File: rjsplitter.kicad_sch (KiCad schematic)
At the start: 8 parts, among them J1 8P8C, J2 8P8C, J3 8P8C, J4 8P8C, J5 8P8C

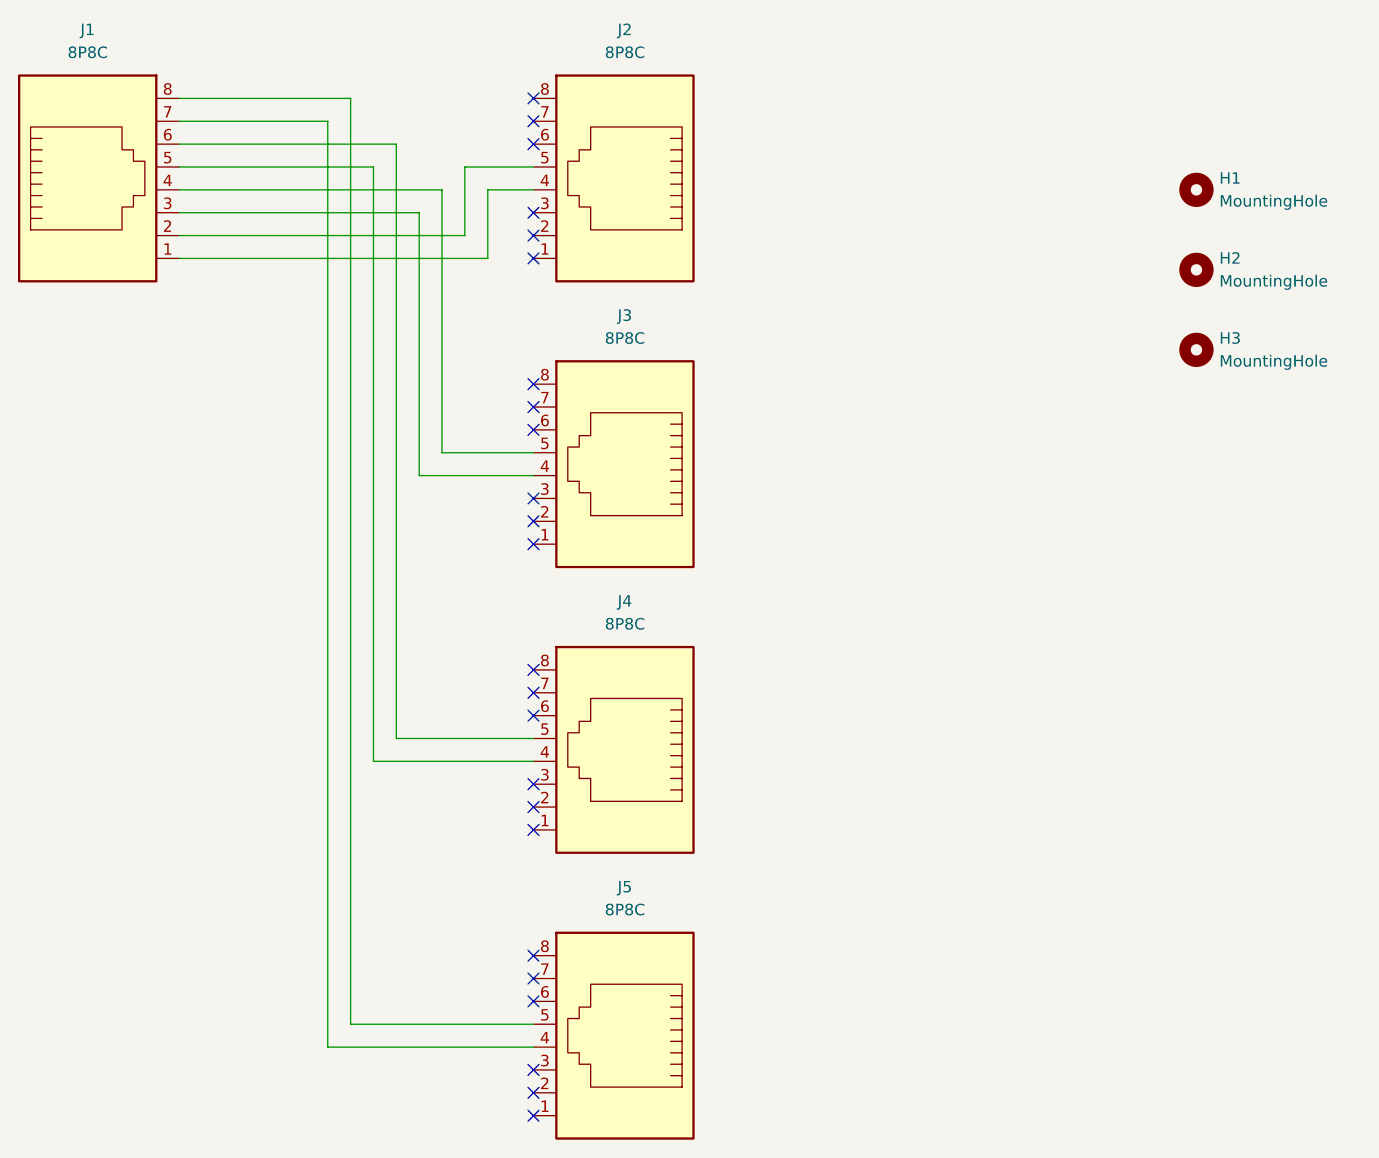
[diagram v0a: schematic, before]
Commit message: Switch to a mix of RJ45 and RJ11.
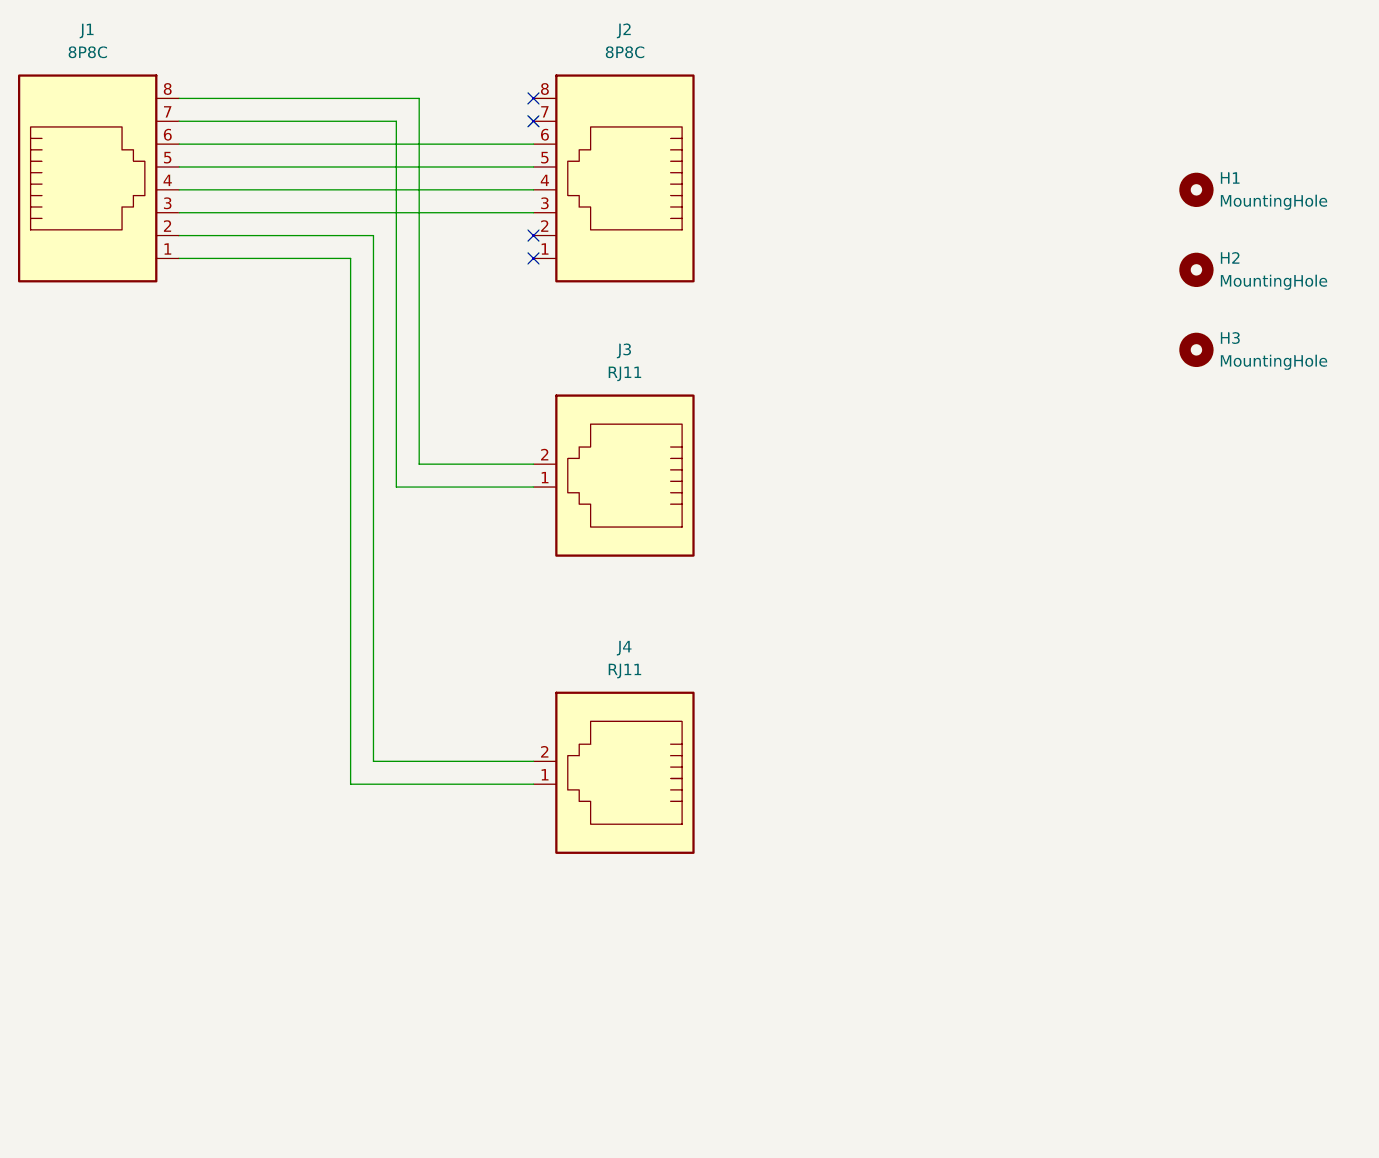
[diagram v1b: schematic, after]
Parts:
- removed J3, J4, J5: 8P8C, Connector_RJ:RJ45_Amphenol_54602-x08_Horizontal, symbol Connector:8P8C
- added J3, J4: RJ11, kicad:AMPHENOL_54601-906WPLF, symbol Connector:RJ11
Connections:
- net at J1.1: now also J4.1; no longer J2.4
- net at J1.2: now also J4.2; no longer J2.5
- net at J1.3: now also J2.3
- net at J1.4: now also J2.4
- net at J1.5: now also J2.5
- net at J1.6: now also J2.6
- net at J1.7: now also J3.1
- net at J1.8: now also J3.2
- no-connect marks 24 -> 4
